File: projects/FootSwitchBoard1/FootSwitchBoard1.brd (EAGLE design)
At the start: 100 x 80 mm, 10 parts

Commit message: Board updates.
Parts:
- added BD_V+, BD_V/2, GND, GND1, GND2, GND3, GND4, GND5, JK_V+: WIREPAD2,54/0,8, wirepad:2,54/0,8
- added C2: (no value), gm-caps-film-box:072X035
- added C3: (no value), gm-caps-electro-pol:080_035
- added R3, R4: (no value), gm-resistors:R0207/4
- moved BD_OUT 56.0 mm to (21.7, 23.6)
- moved JK_IN 55.1 mm to (21.2, 14.2)
- moved BD_IN 47.2 mm to (21.6, 33.2)
- moved R1 46.8 mm to (17.1, 27.3), turned to 90 degrees
- moved JK_OUT 46.1 mm to (20.9, 6.21)
- moved C1 44.7 mm to (5.71, 25.1), turned to 180 degrees
- moved D1 36.3 mm to (10.9, 33.6)
- moved R2 32.7 mm to (13.6, 38.5), turned to 180 degrees
- moved D2 32.4 mm to (13.7, 42.3)
- moved U$1 31.0 mm to (9.41, 10.2)
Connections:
- new net N$10: BD_V/2.1, C3.+, R3.1, R4.2
- new net N$11: C1.-, C2.2, C3.-, GND.1, GND1.1, GND2.1, GND3.1, GND4.1, GND5.1, R4.1, U$1.A1, U$1.A2, U$1.B1
- new net N$9: BD_V+.1, C1.+, C2.1, D1.A, R2.2, R3.2
- net N$7: now also D2.A, JK_V+.1; no longer U$1.A1, U$1.A2, U$1.B1
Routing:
- net N$11: track 0.00 -> 111.9 mm
- net N$9: track 0.00 -> 46.8 mm
- net N$4: track 0.00 -> 28.5 mm
- net N$3: track 0.00 -> 22.2 mm
- net N$10: track 0.00 -> 21.6 mm
- net N$1: track 0.00 -> 21.6 mm
- net N$2: track 0.00 -> 15.5 mm
- net N$8: track 0.00 -> 10.4 mm
- net N$6: track 0.00 -> 7.94 mm
- net N$7: track 0.00 -> 6.55 mm
- net N$5: track 0.00 -> 5.45 mm
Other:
- board size 100 x 80 mm -> 50 x 50 mm

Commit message: Board layout in progress.
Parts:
- removed BD_IN, BD_OUT, BD_V+, BD_V/2, GND, GND1, GND2, GND3, GND4, GND5, JK_IN, JK_OUT, JK_V+: WIREPAD2,54/0,8, wirepad:2,54/0,8
- added -9, 18, 9IN1, 9IN2, BDI, BDO, BDO1, BDV, G0, G1, G2, G3, G4, G5, G6, GD, GN, JKI, JKO, V/2, VIN: WIREPAD2,15/1,0, wirepad:2,15/1,0
- added C4, C5, C6, C7: 10u, gm-caps-electro-pol:050_020
- added D3: (no value), gm-diodes:DO35-3
- added D5, D6: (no value), gm-diodes:DO41-3
- added R5: (no value), gm-resistors:1003
- added TC1044S, TC1044S1: (no value), ic-package:SOCKET-08
- R1, R2, R3, R4: device gm-resistors:R0207/4 -> gm-resistors:R0207/3
- moved R1 20.9 mm to (37.9, 26.3)
- moved C3 20.8 mm to (4.75, 25.1)
- moved C2 9.30 mm to (17.1, 33.1), turned to 90 degrees
- moved C1 8.64 mm to (14.3, 25.1)
- moved R3 2.73 mm to (4.42, 34.0), turned to 90 degrees
- moved R4 2.59 mm to (4.42, 34.0), turned to 270 degrees
- moved D1 2.16 mm to (9.35, 32.0)
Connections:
- new net -9GND: C7.+, GN.1, TC1044S1.3
- new net 18VGND: C4.-, C5.-, GD.1, TC1044S.3, TC1044S.5
- new net N$12: D3.A, R5.2
- new net N$13: 9IN2.1, D5.A, TC1044S.1, TC1044S.8
- new net N$14: C4.+, D5.C, D6.A
- new net N$15: 18.1, C5.+, D6.C
- new net N$16: 9IN1.1, TC1044S1.1, TC1044S1.8
- new net N$17: -9.1, C7.-, TC1044S1.5
- new net N$20: C6.+, TC1044S1.2
- new net N$21: C6.-, TC1044S1.4
- net N$1: now also JKI.1; no longer JK_IN.1
- net N$10: now also V/2.1; no longer BD_V/2.1
- net N$11: now also G0.1, G1.1, G2.1, G3.1, G4.1, G5.1, G6.1, R5.1; no longer GND.1, GND1.1, GND2.1, GND3.1, GND4.1, GND5.1
- net N$2: now also JKO.1; no longer JK_OUT.1
- net N$3: now also BDO.1, BDO1.1; no longer BD_OUT.1
- net N$4: now also BDI.1; no longer BD_IN.1
- net N$7: now also VIN.1; no longer JK_V+.1
- net N$9: now also BDV.1, D3.C; no longer BD_V+.1
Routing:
- net N$11: track 111.9 -> 10.1 mm
- net N$9: track 46.8 -> 0.00 mm
- net N$4: track 28.5 -> 0.00 mm
- net N$15: track 0.00 -> 28.1 mm
- net 18VGND: track 0.00 -> 24.9 mm
- net N$3: track 22.2 -> 0.00 mm
- net N$10: track 21.6 -> 0.00 mm
- net N$13: track 0.00 -> 18.7 mm
- net N$17: track 0.00 -> 18.7 mm
- net -9GND: track 0.00 -> 17.9 mm
- net N$2: track 15.5 -> 0.00 mm
- net N$16: track 0.00 -> 12.2 mm
- net N$14: track 0.00 -> 11.5 mm
- net N$21: track 0.00 -> 9.26 mm
- net N$1: track 21.6 -> 12.8 mm
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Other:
- board text added: "DOUBLER BD"
- board text added: "FOOTSWITCH BD"
- board text added: "INVERTER BD"
- board text added: "Rev 1.0"
- board text added: "Rev 1.0 GJC"

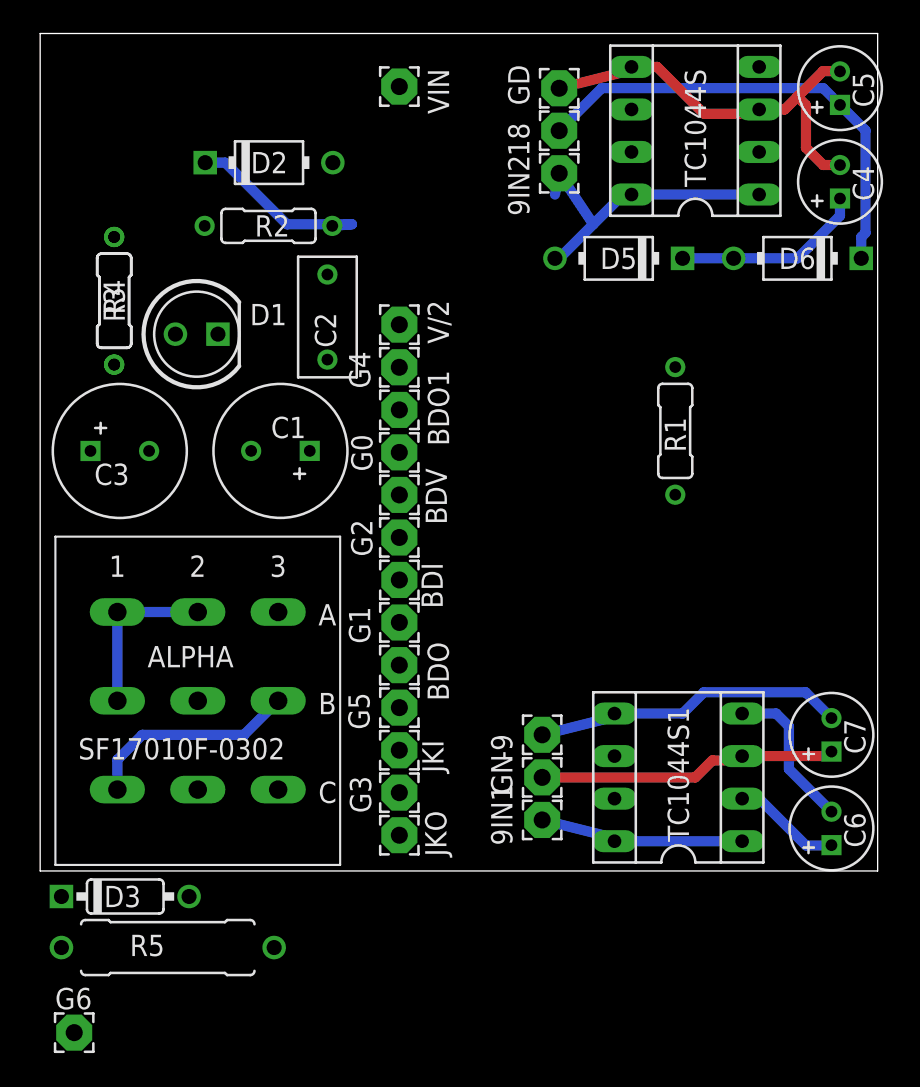
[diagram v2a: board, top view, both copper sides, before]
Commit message: Implemented combined inverter/doubler board.
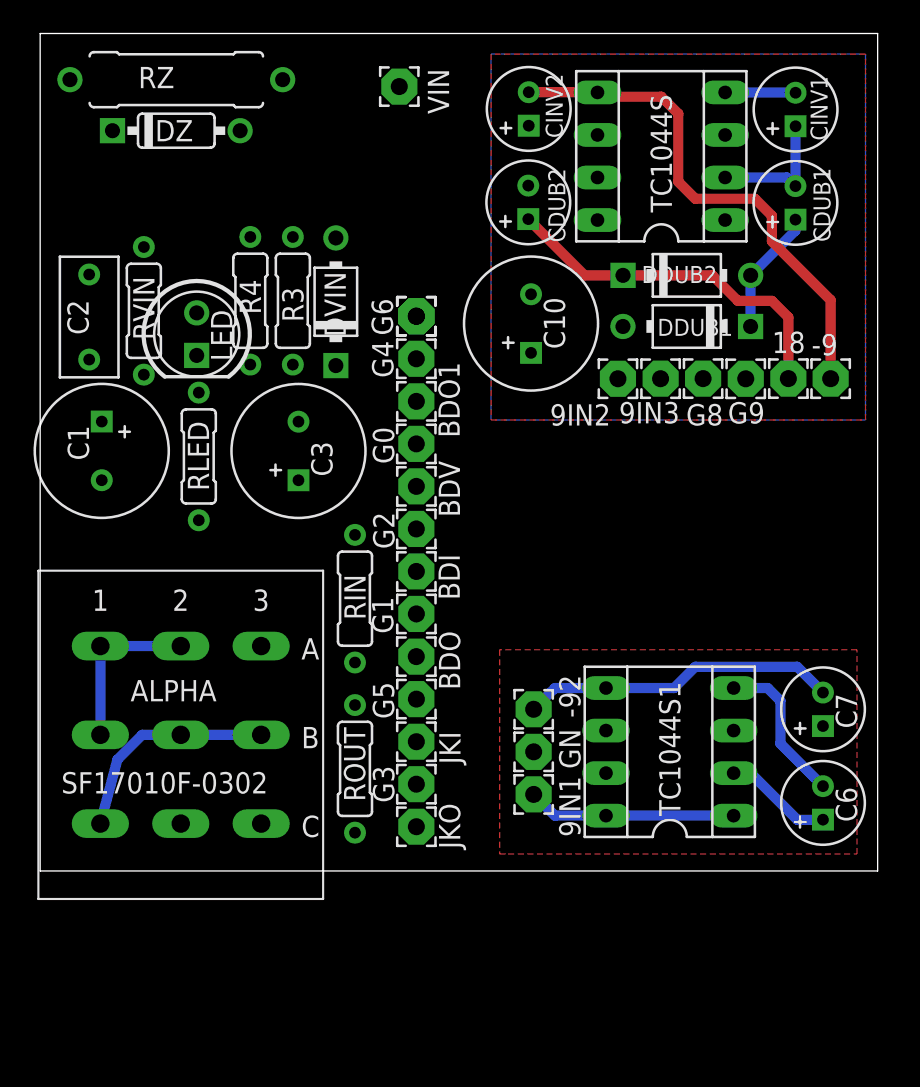
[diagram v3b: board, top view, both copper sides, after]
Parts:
- removed C4, C5: 10u, gm-caps-electro-pol:050_020
- removed D2, D5, D6: (no value), gm-diodes:DO41-3
- removed D3: (no value), gm-diodes:DO35-3
- removed GD: WIREPAD2,15/1,0, wirepad:2,15/1,0
- removed R1, R2: (no value), gm-resistors:R0207/3
- removed R5: (no value), gm-resistors:1003
- added -92, 9IN3, G8, G9: WIREPAD2,15/1,0, wirepad:2,15/1,0
- added C10: 100u, gm-caps-electro-pol:080_035
- added CDUB1, CDUB2, CINV1, CINV2: 10u, gm-caps-electro-pol:050_020
- added DDUB1, DDUB2, DVIN: (no value), gm-diodes:DO41-3
- added DZ: (no value), gm-diodes:DO35-3
- added RIN, RLED, ROUT, RVIN: (no value), gm-resistors:R0207/3
- added RZ: (no value), gm-resistors:1003
- C1, C3: value (none) -> 100u
- C2: value (none) -> 100n
- moved G6 47.4 mm to (22.5, 33.1), turned to 90 degrees
- moved -9 27.4 mm to (47.2, 29.4), turned to 0 degrees
- moved 18 20.2 mm to (44.7, 29.4), turned to 90 degrees
- moved C2 14.2 mm to (2.93, 33.1)
- moved 9IN2 12.8 mm to (34.5, 29.4), turned to 270 degrees
- moved C3 10.7 mm to (15.4, 25.1), turned to 90 degrees
- moved C1 10.7 mm to (3.68, 25.1), turned to 270 degrees
- moved R3 10.7 mm to (15.1, 34.0)
- moved R4 8.13 mm to (12.5, 34.0)
- moved TC1044S 2.54 mm to (37.1, 42.7)
- moved U$1 2.27 mm to (8.39, 8.13)
- moved 9IN1 1.61 mm to (29.5, 4.57)
- moved C6 1.61 mm to (46.7, 4.06)
- moved GN 1.61 mm to (29.5, 7.11)
- moved TC1044S1 1.61 mm to (37.6, 7.11)
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- renumbered D1 to LED
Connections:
- removed net 18VGND: C4.-, C5.-, GD.1, TC1044S.3, TC1044S.5
- removed net N$14: C4.+, D5.C, D6.A
- removed net N$9: BDV.1, C1.+, C2.1, D3.C, LED.A, R2.2, R3.2
- new net 9INDUBINV: 9IN2.1, 9IN3.1, C10.+, DDUB1.A, TC1044S.1, TC1044S.8
- new net DDUB2: CDUB1.+, DDUB1.C, DDUB2.A
- new net GDUBINV: C10.-, CDUB2.-, CINV2.+, G8.1, G9.1
- new net N$18: DVIN.C, DZ.C, LED.A, R3.2, RVIN.1
- new net N$19: -9.1, CINV2.-, TC1044S.5
- new net N$22: 18.1, CDUB2.+, DDUB2.C
- net N$1: now also RIN.2
- net N$11: now also RIN.1, ROUT.1, RZ.1; no longer R5.1
- net N$12: now also DZ.A, RZ.2; no longer D3.A, R5.2
- net N$13: now also CDUB1.-, CINV1.+, TC1044S.2; no longer 9IN2.1, D5.A, TC1044S.1, TC1044S.8
- net N$15: now also CINV1.-, TC1044S.4; no longer 18.1, C5.+, D6.C
- net N$17: now also -92.1; no longer -9.1
- net N$2: now also ROUT.2
- net N$5: now also RLED.2; no longer R1.2
- net N$6: now also RLED.1; no longer R1.1
- net N$7: now also DVIN.A; no longer D2.A
- net N$8: now also BDV.1, C1.+, C2.1, RVIN.2; no longer D2.C, R2.1
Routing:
- net N$19: track 0.00 -> 31.1 mm, vias 0 -> 1
- net 18VGND: track 24.9 -> 0.00 mm
- net N$15: track 28.1 -> 4.21 mm
- net N$22: track 0.00 -> 21.6 mm
- net -9GND: track 17.9 -> 0.38 mm
- net N$14: track 11.5 -> 0.00 mm
- net N$8: track 11.5 -> 0.00 mm
- net N$13: track 18.7 -> 7.99 mm
- net DDUB2: track 0.00 -> 7.49 mm
- added copper zone on layer 1, net -9GND
- added copper zone on layer 1, net 9INDUBINV
- added copper zone on layer 16, net GDUBINV
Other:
- board text added: "DOUBLER/INVERTER"
- board text removed: "DOUBLER BD"
- board text removed: "Rev 1.0"

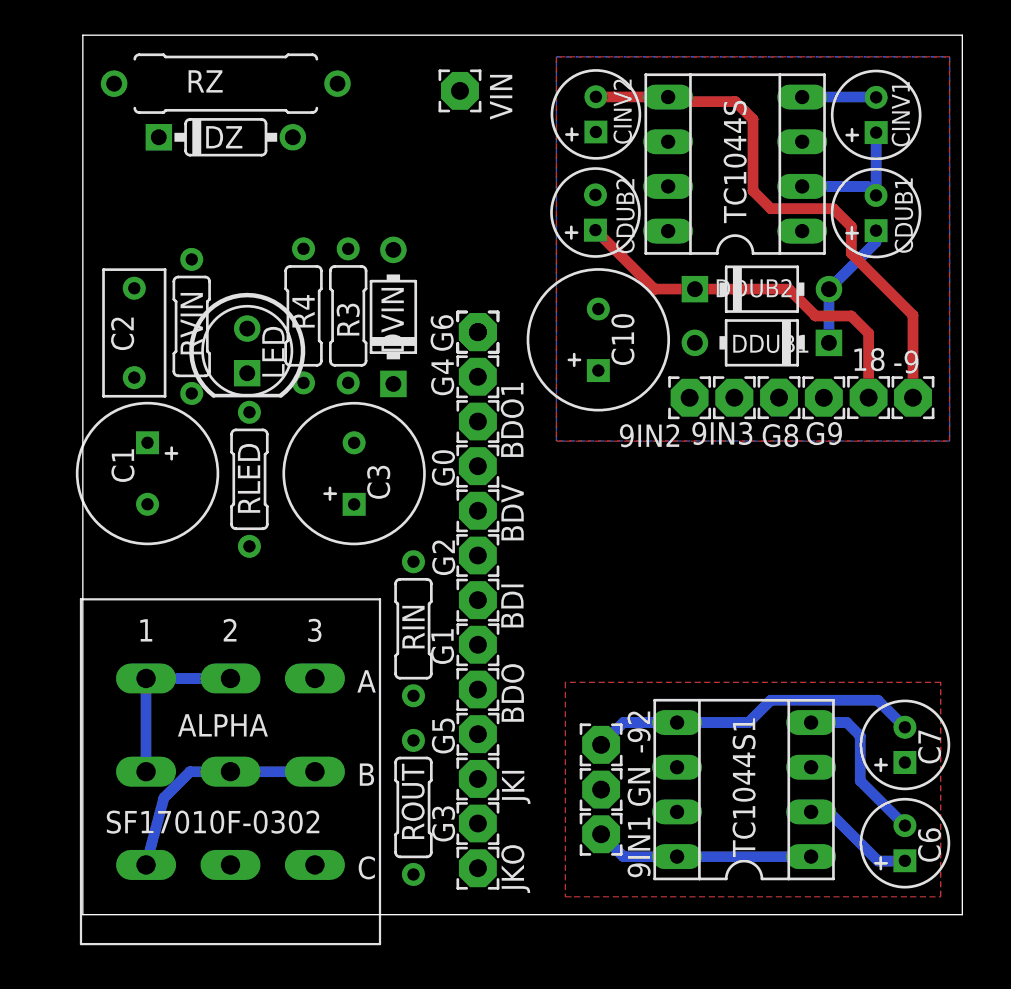
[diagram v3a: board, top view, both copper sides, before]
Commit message: Circuit mods, new OVP UVP circuit added.
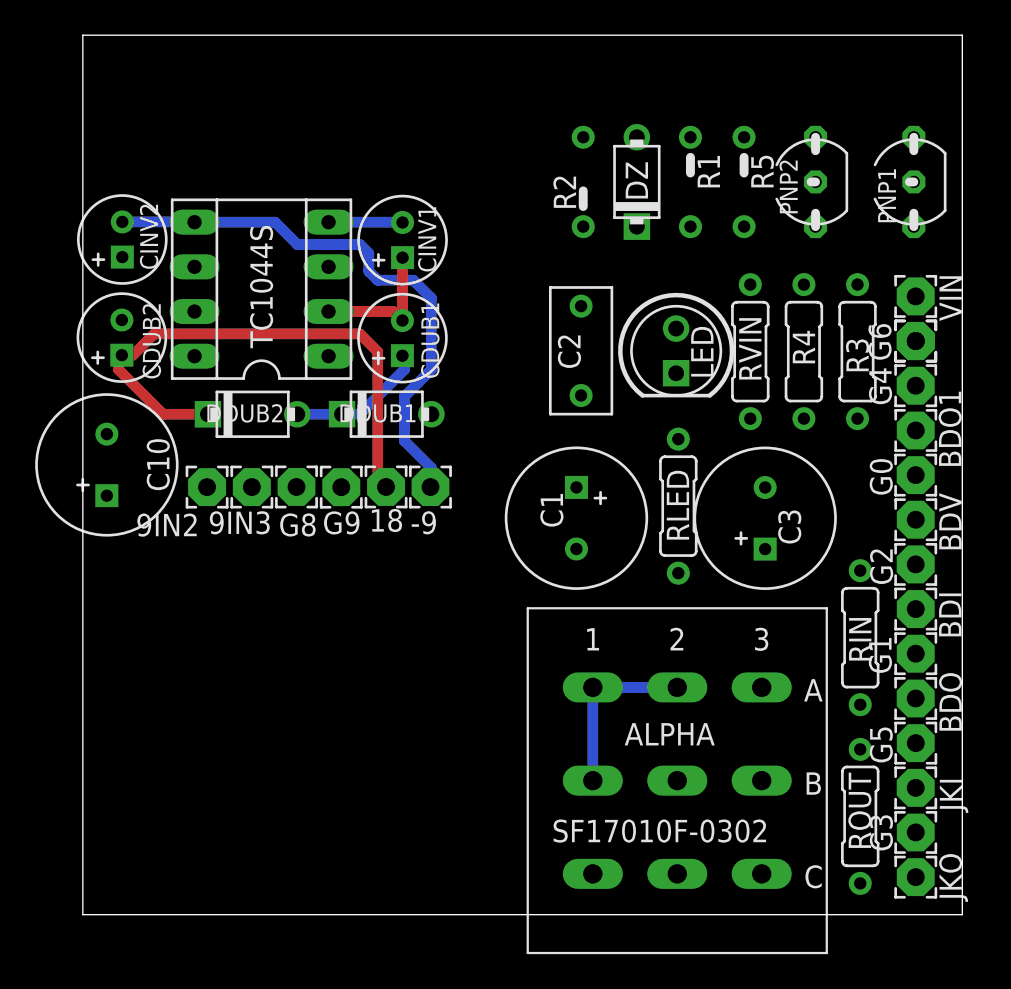
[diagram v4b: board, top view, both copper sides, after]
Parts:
- removed -92, 9IN1, GN: WIREPAD2,15/1,0, wirepad:2,15/1,0
- removed C6, C7: 10u, gm-caps-electro-pol:050_020
- removed DVIN: (no value), gm-diodes:DO41-3
- removed RZ: (no value), gm-resistors:1003
- removed TC1044S1: (no value), ic-package:SOCKET-08
- added PNP1, PNP2: 2N3906-, gm-trans:TO92-
- added R1, R2: 10k, gm-resistors:R0207/2V
- added R5: 100k, gm-resistors:R0207/2V
- DDUB1, DDUB2: value (none) -> 1N58172; device gm-diodes:DO41-3 -> gm-diodes:DO41-2
- DZ: device gm-diodes:DO35-3 -> gm-diodes:DO41-2
- moved RVIN 31.8 mm to (37.9, 32.0)
- moved DDUB2 29.8 mm to (9.65, 28.4)
- moved R3 29.0 mm to (44.0, 32.0)
- moved C10 28.8 mm to (1.37, 25.6)
- moved R4 28.5 mm to (41.0, 32.0)
- moved VIN 28.4 mm to (47.3, 35.1)
- moved -9 27.9 mm to (19.8, 24.3)
- moved 18 27.9 mm to (17.2, 24.3)
- moved 9IN2 27.9 mm to (7.06, 24.3)
- moved 9IN3 27.9 mm to (9.61, 24.3)
- moved G9 27.9 mm to (14.7, 24.3)
- moved G8 27.9 mm to (12.1, 24.3)
- moved CDUB2 27.8 mm to (2.22, 32.8)
- moved TC1044S 27.8 mm to (10.2, 35.6)
- moved CINV2 27.8 mm to (2.24, 38.4)
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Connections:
- removed net -9GND: C7.+, GN.1, TC1044S1.3
- removed net N$11: C1.-, C2.2, C3.-, G0.1, G1.1, G2.1, G3.1, G4.1, G5.1, G6.1, R4.1, RIN.1, ROUT.1, RZ.1, U$1.A1, U$1.A2, U$1.B1
- removed net N$12: DZ.A, RZ.2
- removed net N$16: 9IN1.1, TC1044S1.1, TC1044S1.8
- removed net N$17: -92.1, C7.-, TC1044S1.5
- removed net N$18: DVIN.C, DZ.C, LED.A, R3.2, RVIN.1
- removed net N$20: C6.+, TC1044S1.2
- removed net N$21: C6.-, TC1044S1.4
- removed net N$7: DVIN.A, VIN.1
- removed net N$8: BDV.1, C1.+, C2.1, RVIN.2
- new net N$14: DZ.C, R2.1, R5.1
- new net N$23: PNP1.2, PNP2.1, R1.2
- new net N$24: PNP1.3, PNP2.3, R5.2, VIN.1
- new net N$25: LED.A, PNP1.1, R3.2, RVIN.1
- new net N$9: PNP2.2, R2.2
- net 9INDUBINV: now also BDV.1, C1.+, C2.1, RVIN.2
- net GDUBINV: now also C1.-, C2.2, C3.-, DZ.A, G0.1, G1.1, G2.1, G3.1, G4.1, G5.1, G6.1, R1.1, R4.1, RIN.1, ROUT.1, U$1.A1, U$1.A2, U$1.B1
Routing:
- net N$17: track 19.0 -> 0.00 mm
- net N$1: track 13.1 -> 0.00 mm
- net N$16: track 12.5 -> 0.00 mm
- net N$11: track 10.1 -> 0.00 mm
- net GDUBINV: track 0.00 -> 10.1 mm
- net N$21: track 9.26 -> 0.00 mm
- net N$22: track 21.6 -> 30.4 mm
- net N$20: track 6.50 -> 0.00 mm
- net N$19: track 31.1 -> 32.0 mm, vias 1 -> 0
- net DDUB2: track 7.49 -> 7.99 mm
- removed copper zone on layer 1, net -9GND
- removed copper zone on layer 1, net 9INDUBINV
- removed copper zone on layer 16, net GDUBINV
